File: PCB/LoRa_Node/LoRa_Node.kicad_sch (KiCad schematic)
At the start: 63 parts, among them IC1 SPX5205M5-L/TR, IC2 SPX5205M5-L/TR, J1 Conn_01x04_Socket, J2 Conn_01x02_Pin, J3 UF.L, J4 2x5_2.00mm, J6 Conn_01x06_Socket, J7 Conn_01x03_Socket, SW1 SW_SPST, U1 BME280, U2 RFM95W-868S2, U3 STM32F103C8Tx, U4 SIM800L-CORE, Y1 12MHz, Y2 32.768kHz

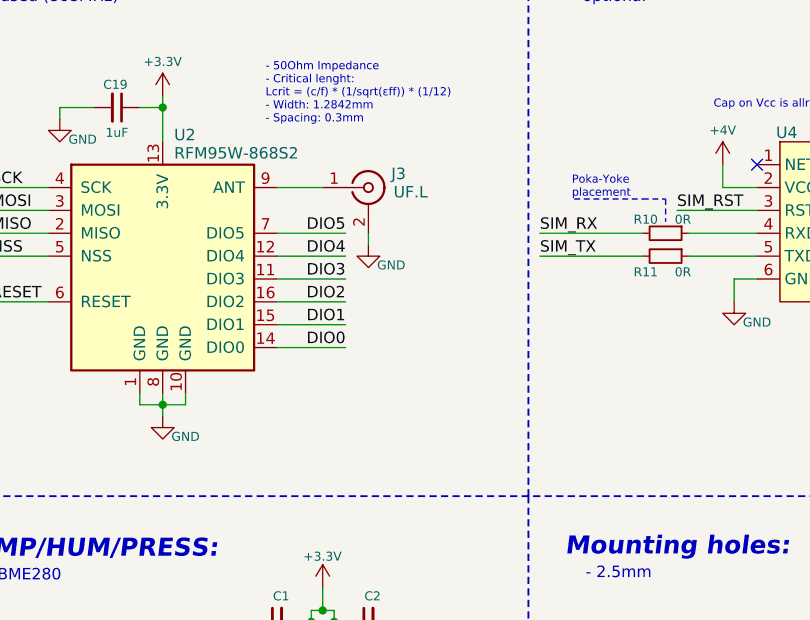
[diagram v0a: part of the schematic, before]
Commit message: Update
PCB: added pull-downs on IRQ pins, SW: stable EXTI, reliable measurements
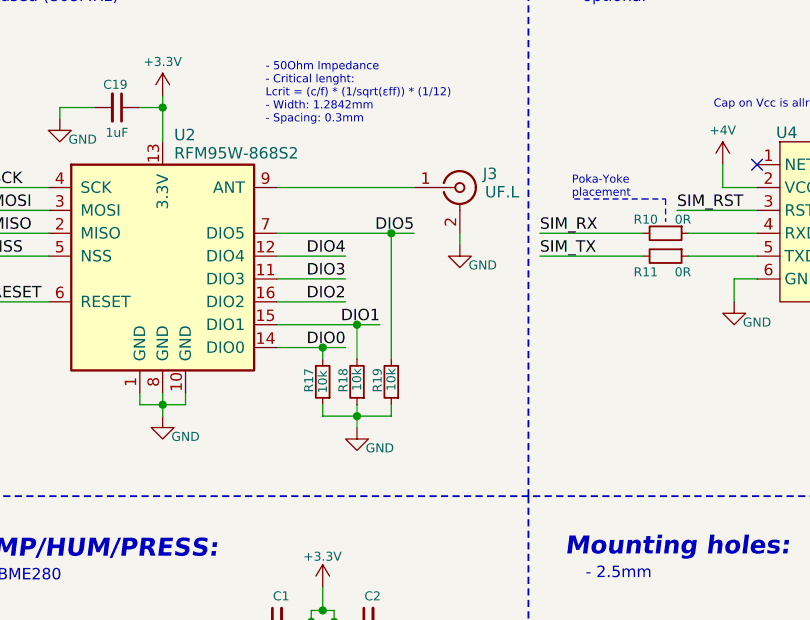
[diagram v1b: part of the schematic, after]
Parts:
- added R17, R18, R19: 10k, Resistor_SMD:R_0603_1608Metric, symbol Device:R_Small
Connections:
- net DIO0: now also R17.2
- net DIO1: now also R18.2
- net DIO5: now also R19.2
- net GND: now also R17.1, R18.1, R19.1
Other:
- company: (none) -> Tinta T.
- title: LoRa node (SIM) -> Greenhouse LoRa node (SIM)
- moved on the sheet: J3

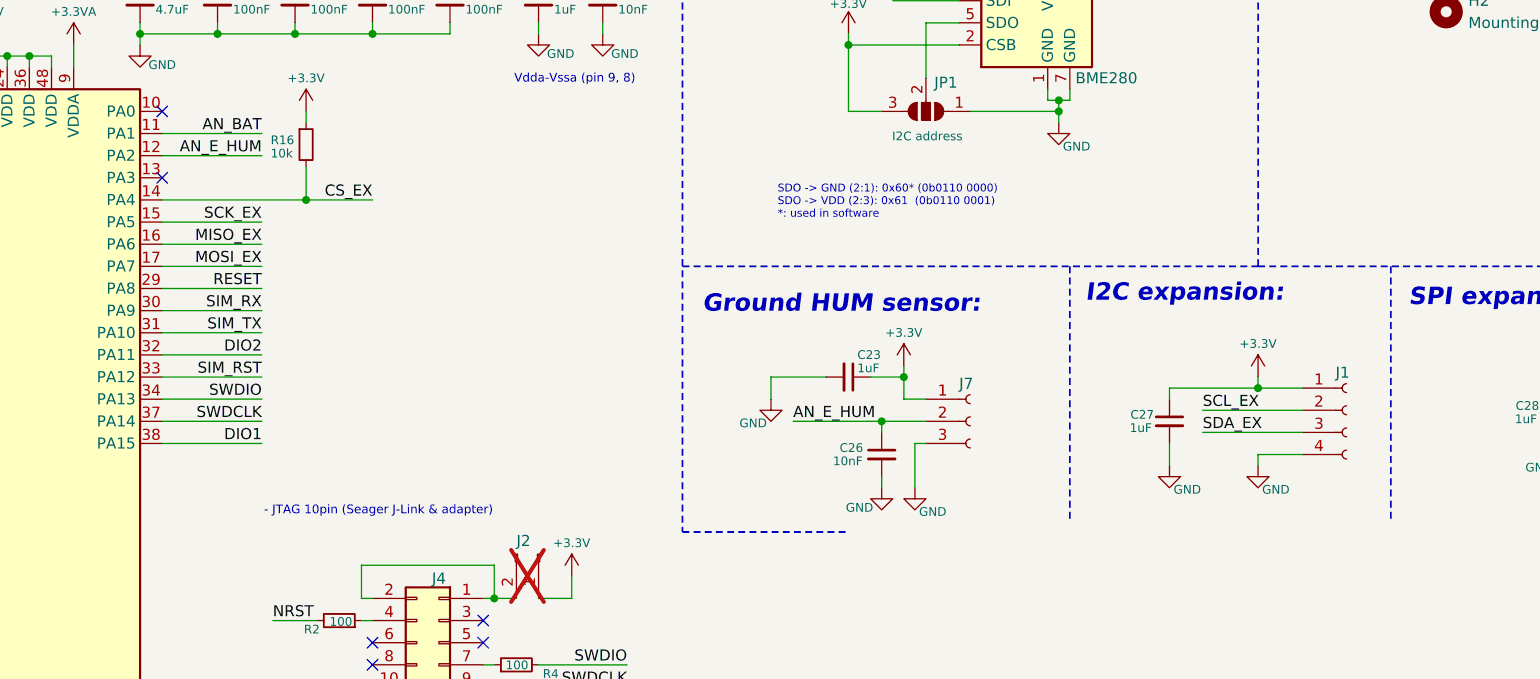
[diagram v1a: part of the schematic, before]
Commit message: Update
Humidity probe is rewired from the 3v3 to MCU pin for power
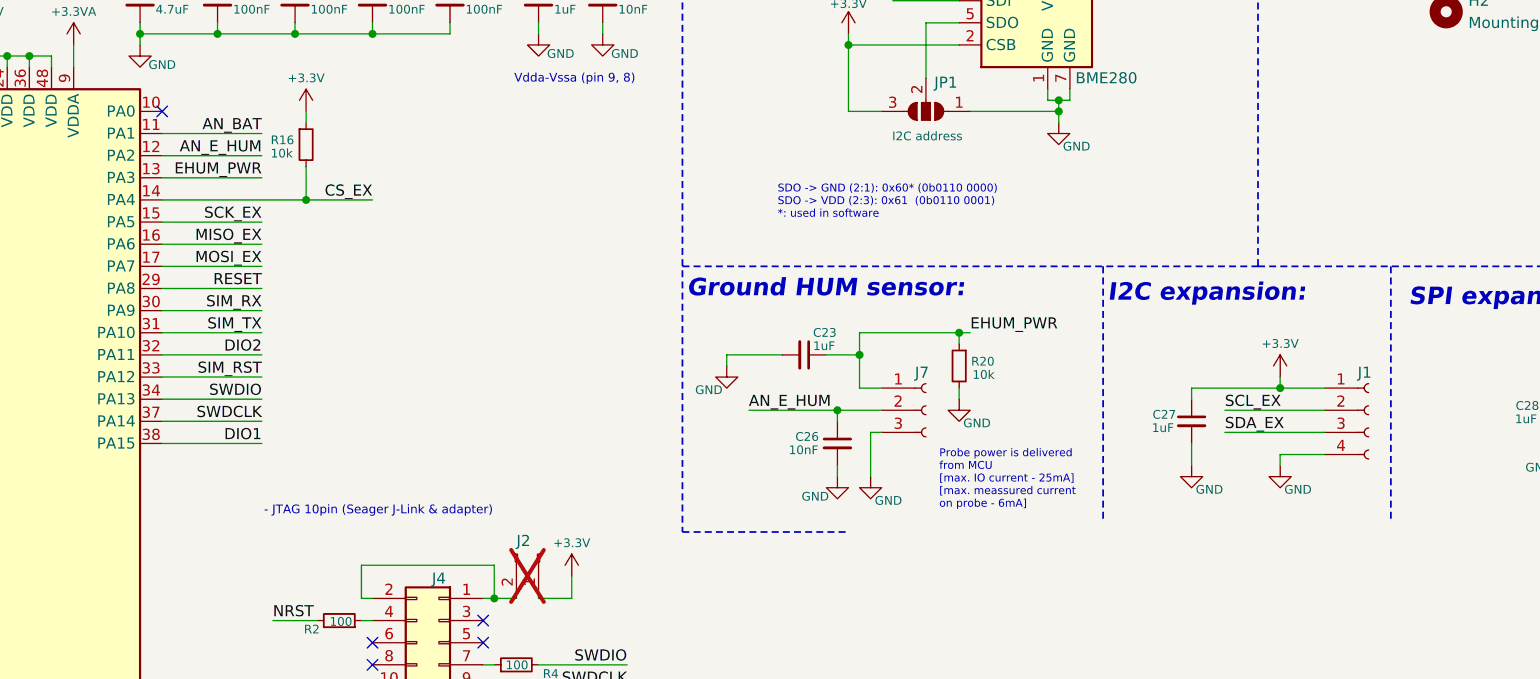
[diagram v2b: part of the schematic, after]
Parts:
- added R20: 10k, Resistor_SMD:R_0603_1608Metric, symbol Device:R_Small
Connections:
- net +3.3V: no longer C23.1, J7.1 (Pin_1)
- net GND: now also R20.2
- net EHUM_PWR: now reaches U3.13 (PA3)
- net EHUM_PWR: now also C23.1, J7.1 (Pin_1), R20.1
- no-connect marks 14 -> 13
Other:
- note added: "Probe power is delivered from MCU [max. IO current - 25mA] [max. meassured current on probe - 6mA]"
- moved on the sheet: C23, C26, C27, J1, J7

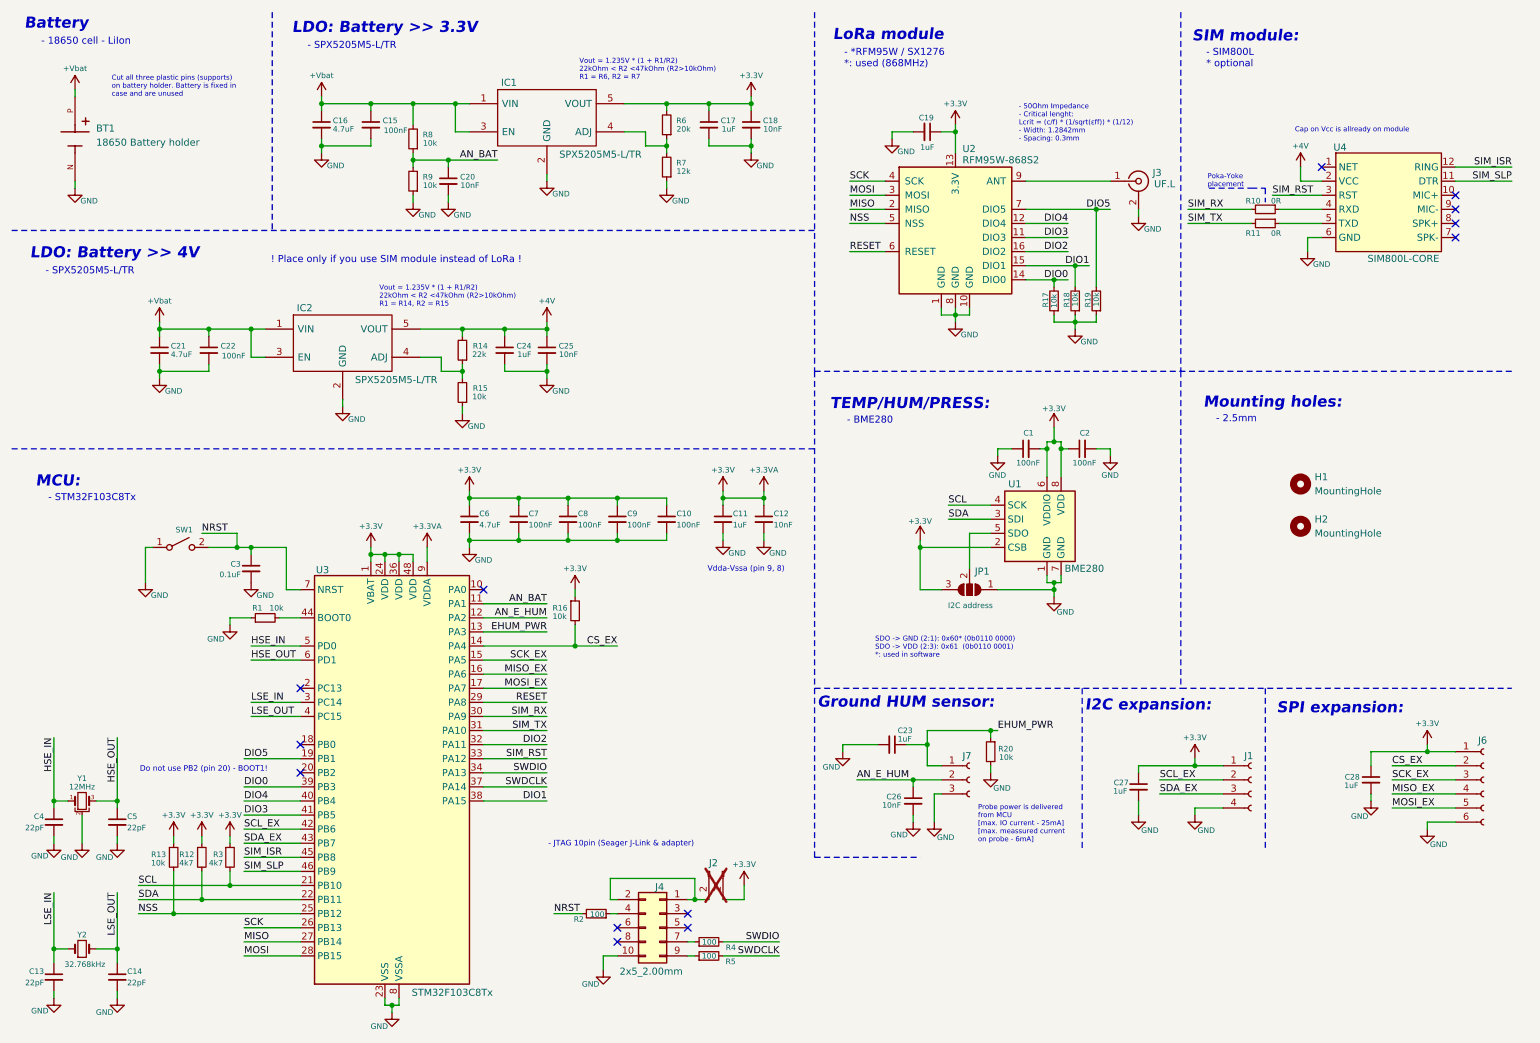
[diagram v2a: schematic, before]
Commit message: Update:
4V bus update (step-up converter)
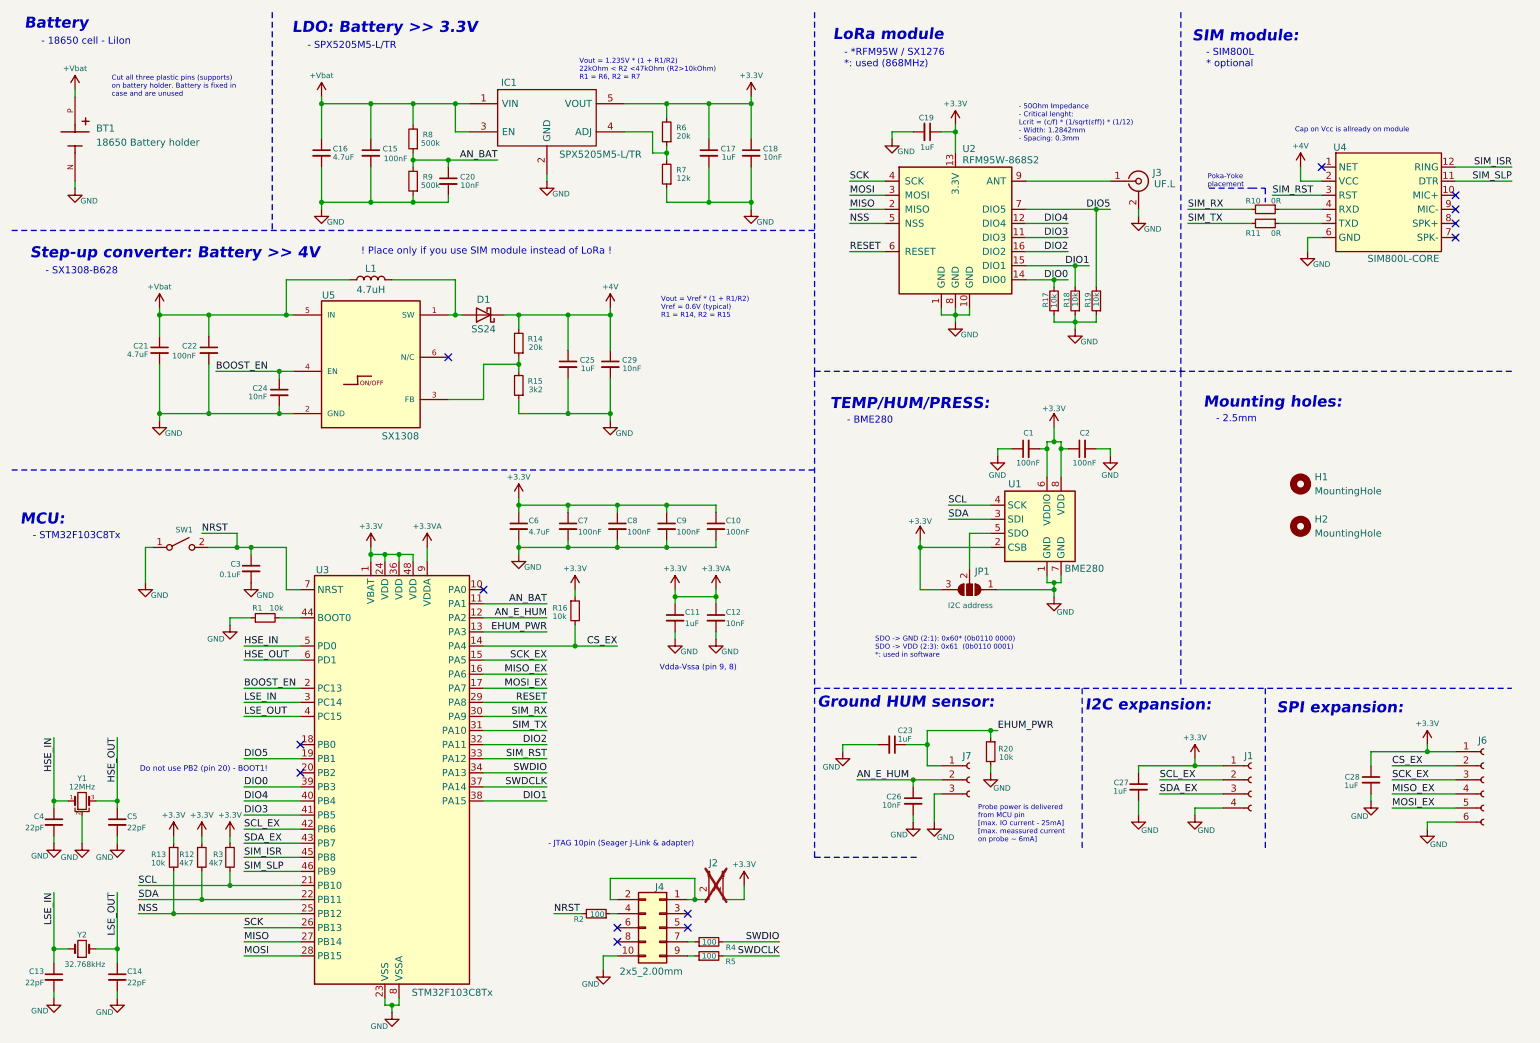
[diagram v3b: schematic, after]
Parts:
- removed IC2: SPX5205M5-L/TR, SOT95P280X145-5N, symbol SPX5205M5-L-3-3_TR:SPX5205M5-L-3-3_TR
- added C29: 10nF, Capacitor_SMD:C_0603_1608Metric, symbol Device:C_Small
- added D1: SS24, Diode_SMD:D_SMA, symbol Diode:SS24
- added L1: 4.7uH, Inductor_SMD:L_Cenker_CKCS4020, symbol Device:L
- added U5: SX1308, SX1308:SOT-23-6, symbol SX1308:SX1308
- C24: value 1uF -> 10nF
- C25: value 10nF -> 1uF
- R14: value 22k -> 20k
- R15: value 10k -> 3k2
- R8, R9: value 10k -> 500k
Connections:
- net +4V: now also C29.1, D1.1 (K); no longer C24.1
- net +Vbat: now also L1.1, U5.5 (IN)
- net GND: now also C29.2, U5.2 (GND)
- net at R14.1, R15.2: now also U5.3 (FB)
- net BOOST_EN: now reaches U3.2 (PC13)
- net BOOST_EN: now also C24.1, U5.4 (EN)
- new net: D1.2 (A), L1.2, U5.1 (SW)
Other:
- note added: "- SX1308-B628"
- note added: "Probe power is delivered from MCU pin [max. IO current - 25mA] [max. meassured current on probe ~ 6mA]"
- note added: "Step-up converter: Battery >> 4V"
- note added: "Vout = Vref * (1 + R1/R2) Vref = 0.6V (typical) R1 = R14, R2 = R15"
- note removed: "LDO: Battery >> 4V"
- note removed: "Probe power is delivered from MCU [max. IO current - 25mA] [max. meassured current on probe - 6mA]"
- note removed: "Vout = 1.235V * (1 + R1/R2) 22kOhm < R2 <47kOhm (R2>10kOhm) R1 = R14, R2 = R15"
- moved on the sheet: C10, C11, C12, C15, C16, C17, C18, C6, C7, C8, C9, R6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

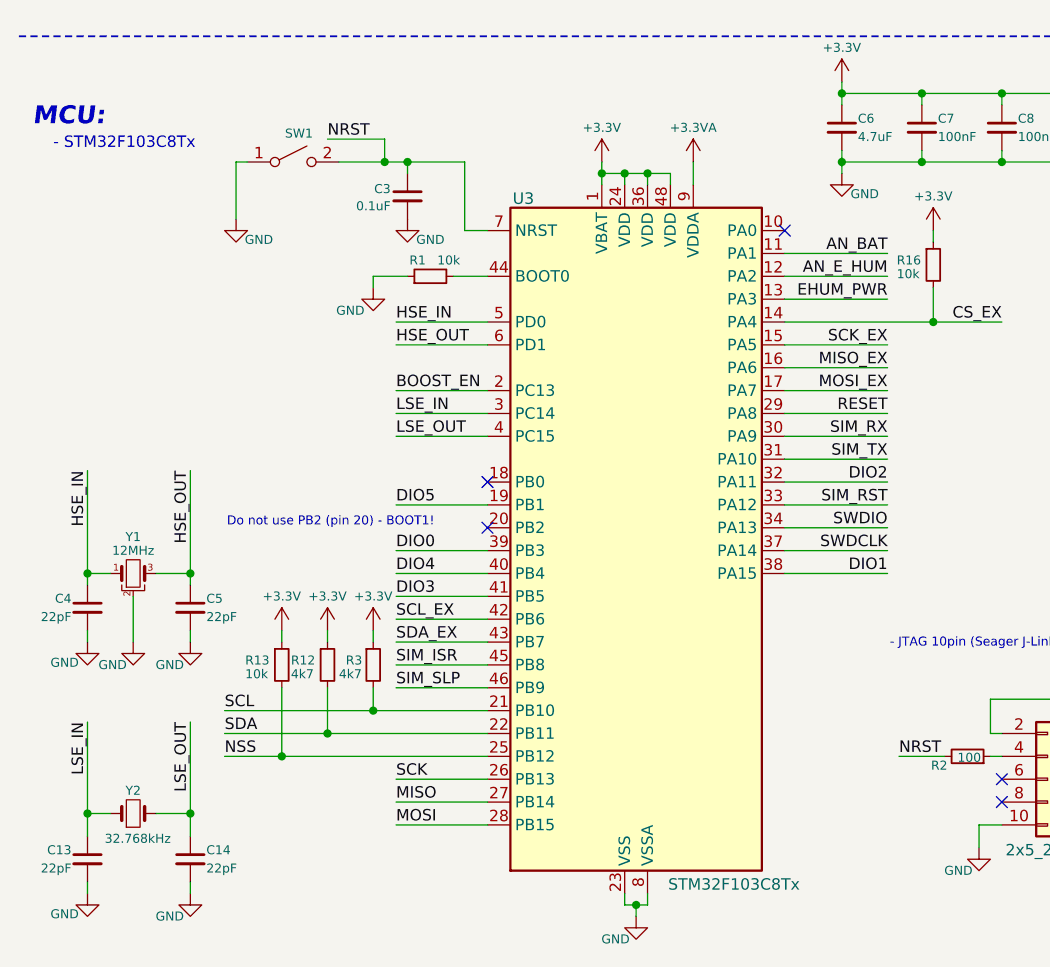
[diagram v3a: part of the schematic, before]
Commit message: added Docker image for all the server applications
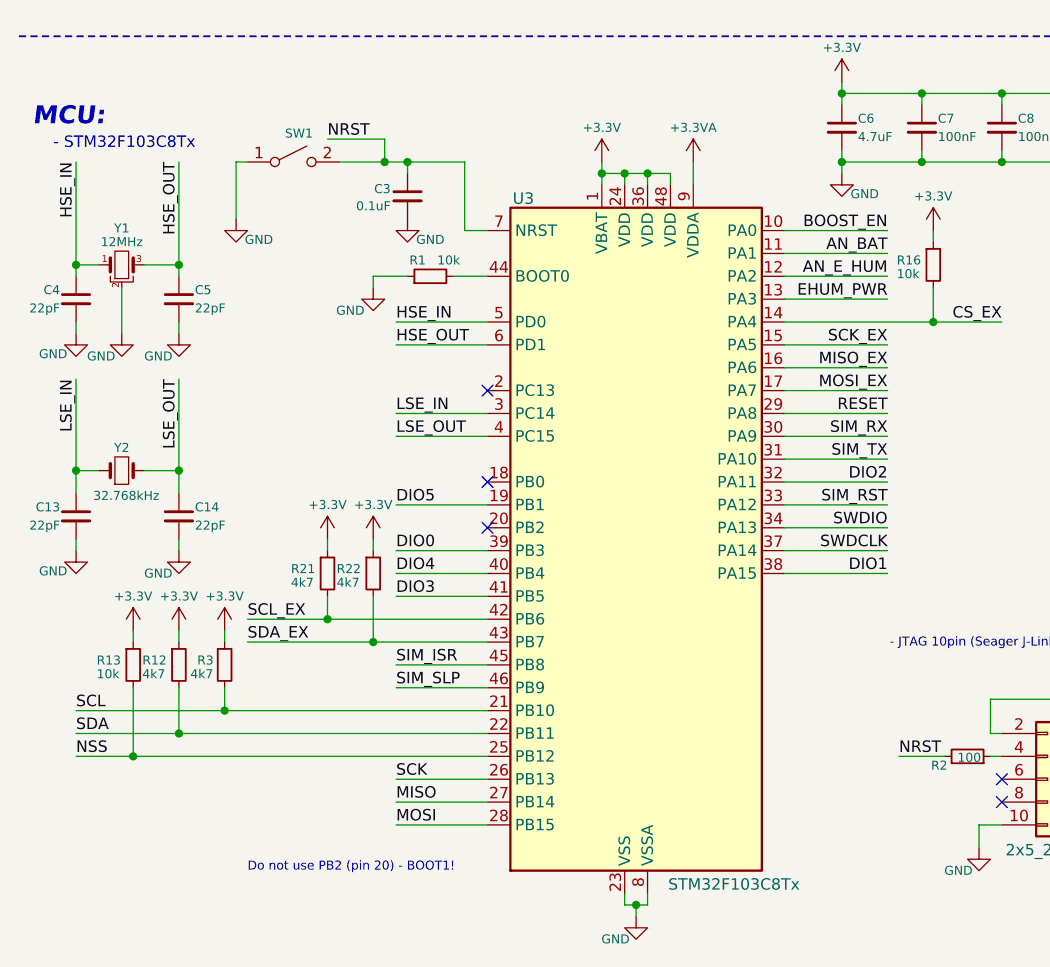
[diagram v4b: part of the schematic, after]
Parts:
- added R21, R22: 4k7, Resistor_SMD:R_0603_1608Metric, symbol Device:R_Small
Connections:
- net +3.3V: now also R21.1, R22.1
- net BOOST_EN: now also U3.10 (PA0); no longer U3.2 (PC13)
- net SCL_EX: now also R21.2
- net SDA_EX: now also R22.2
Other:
- moved on the sheet: C13, C14, C4, C5, R12, R13, R3, Y1, Y2
